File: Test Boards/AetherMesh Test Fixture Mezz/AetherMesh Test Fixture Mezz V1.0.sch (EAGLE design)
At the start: 8 parts, among them J1 POWER_JACKEJ508A, M1 AETHERMESH_MODULEMEZZ-HOLES

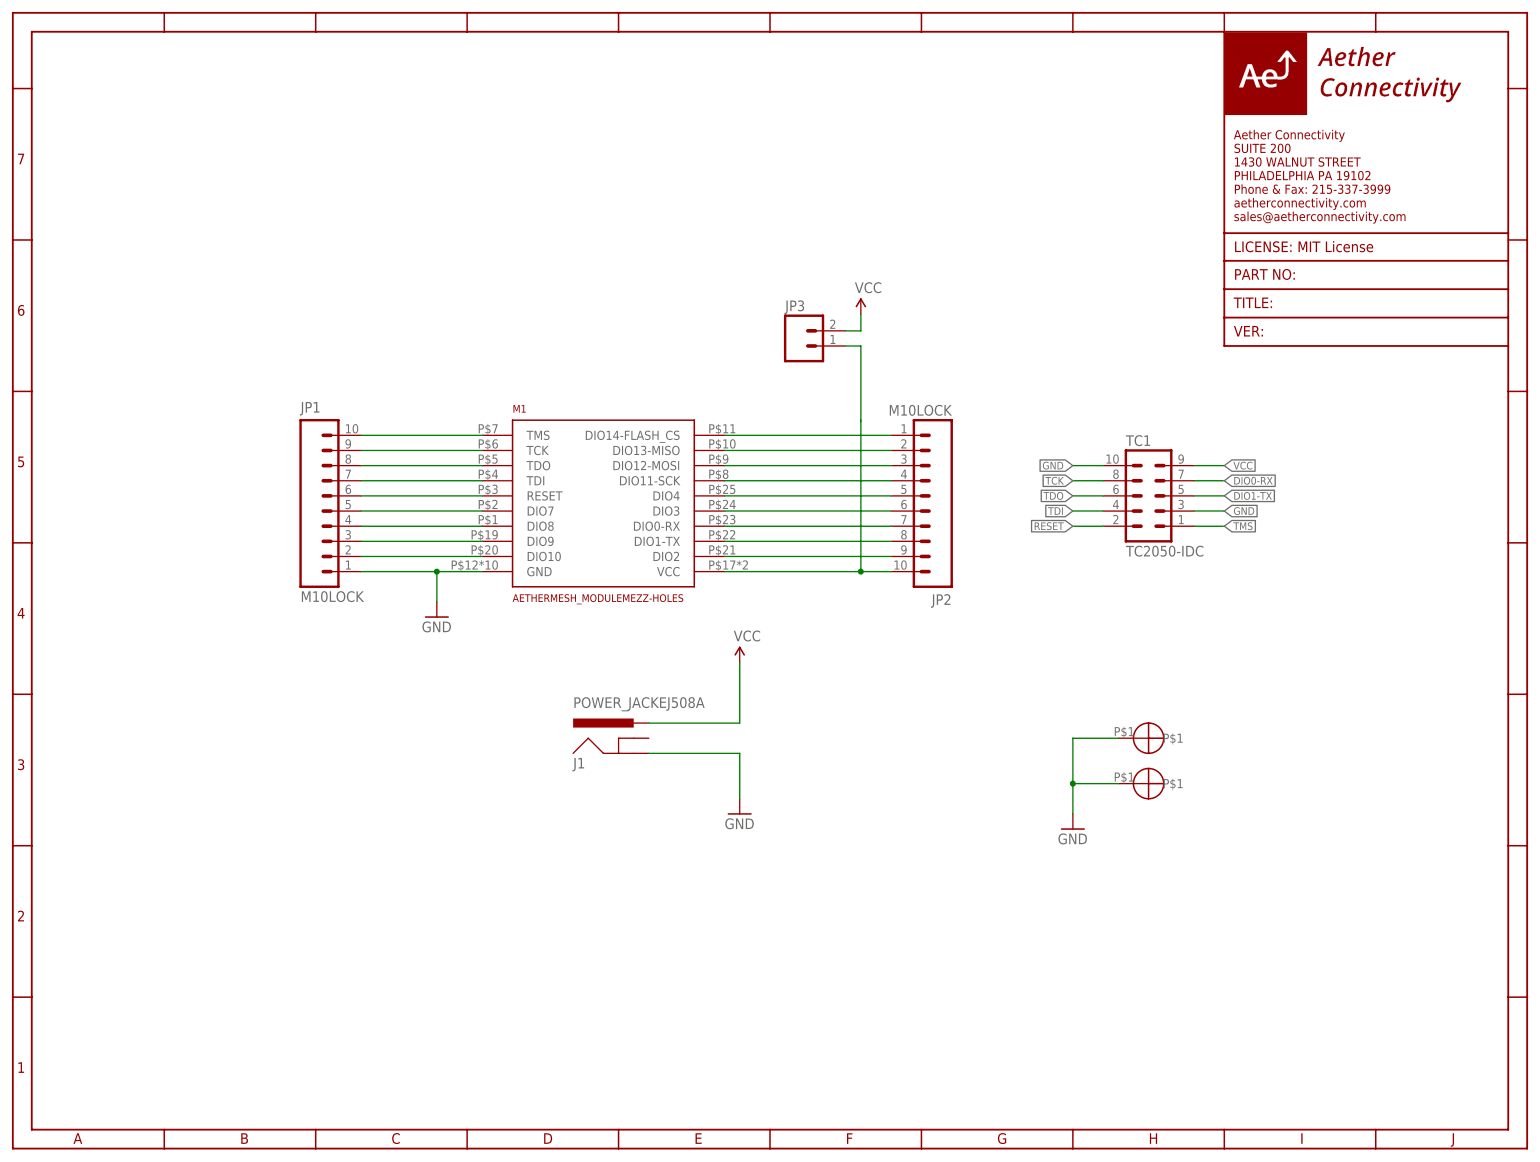
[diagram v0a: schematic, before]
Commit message: Updated reference designs and test boards with latest XDS programmer tag connect header
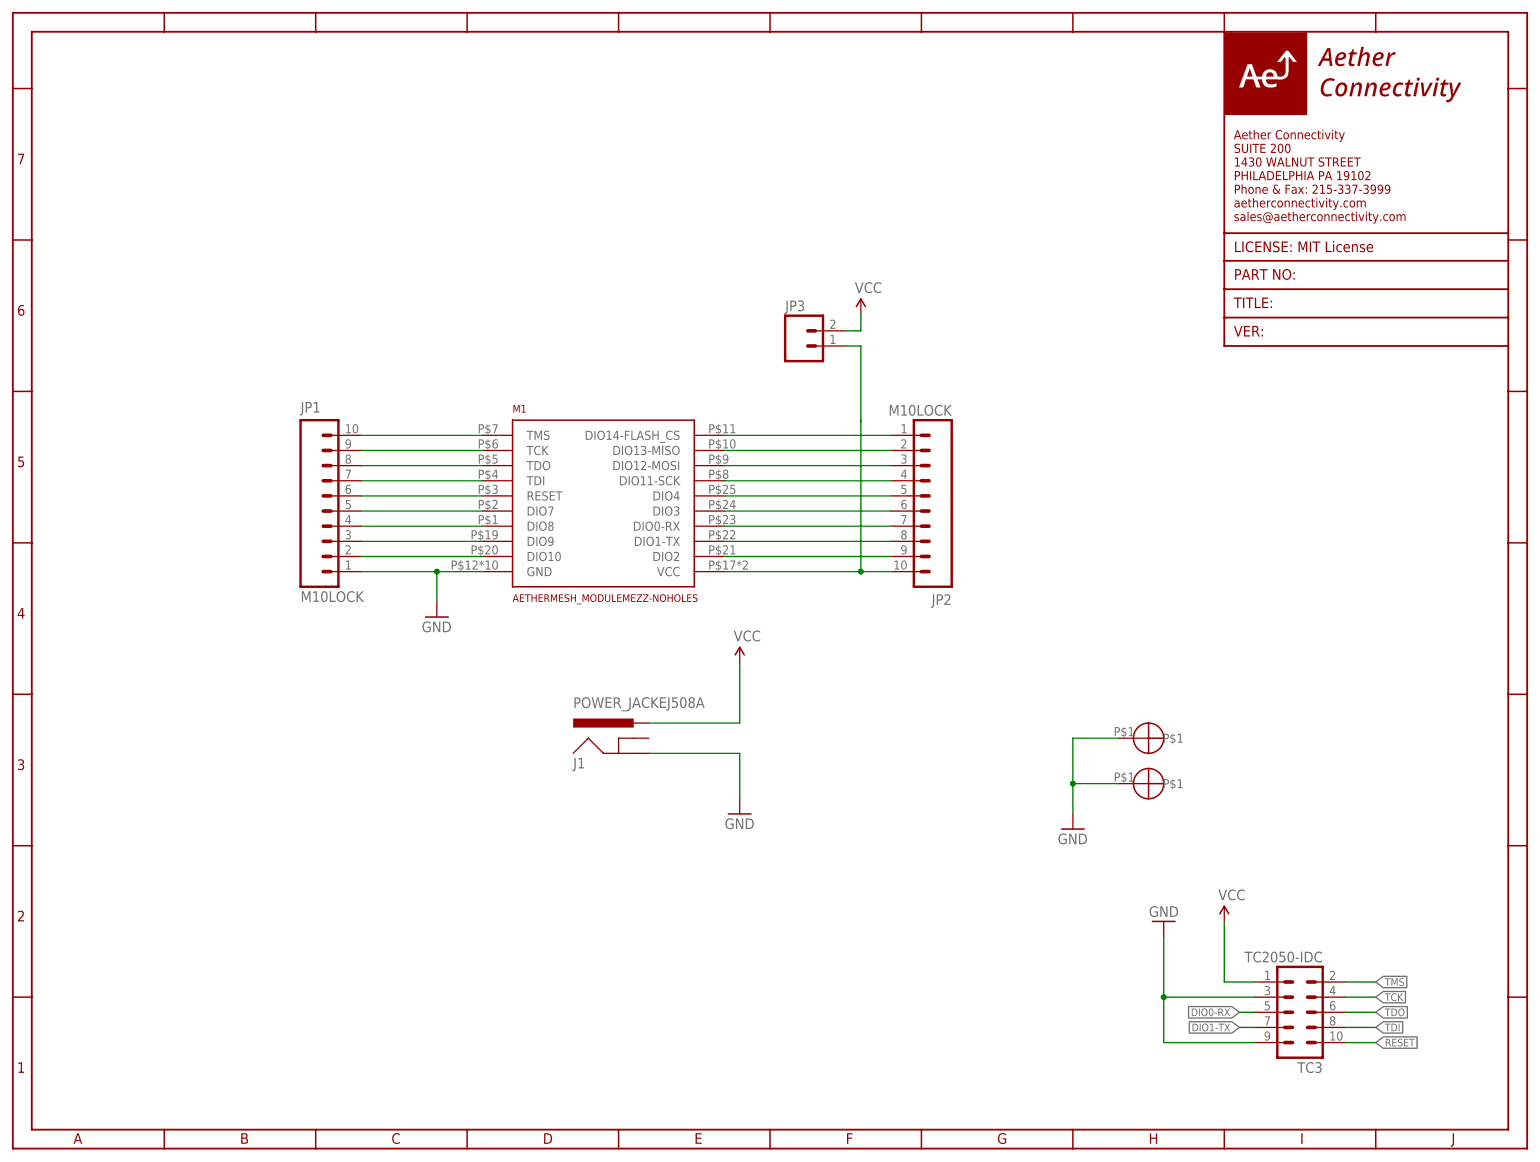
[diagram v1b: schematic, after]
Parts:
- removed TC1: TC2050-IDC, TagConnect:TC2050-IDC
- added TC3: TC2050-IDC, TagConnect:TC2050-IDC
- M1: value AETHERMESH_MODULEMEZZ-HOLES -> AETHERMESH_MODULEMEZZ-NOHOLES; device AetherConnectivity:AETHERMESH_MODULEMEZZ-HOLES -> AetherConnectivity:AETHERMESH_MODULEMEZZ-NOHOLES
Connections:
- net DIO0-RX: now also TC3.5; no longer TC1.7
- net DIO1-TX: now also TC3.7; no longer TC1.5
- net GND: now also TC3.3, TC3.9; no longer TC1.10, TC1.3
- net RESET: now also TC3.10; no longer TC1.2
- net TCK: now also TC3.4; no longer TC1.8
- net TDI: now also TC3.8; no longer TC1.4
- net TDO: now also TC3.6; no longer TC1.6
- net TMS: now also TC3.2; no longer TC1.1
- net VCC: now also TC3.1; no longer TC1.9
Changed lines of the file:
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@@
 <?xml version="1.0" encoding="utf-8"?>
 <!DOCTYPE eagle SYSTEM "eagle.dtd">
-<eagle version="8.4.1">
+<eagle version="9.0.0">
 <drawing>
 <settings>
@@
 <layer number="59" name="tCarbon" color="7" fill="1" visible="no" active="no"/>
 <layer number="60" name="bCarbon" color="7" fill="1" visible="no" active="no"/>
+<layer number="88" name="SimResults" color="9" fill="1" visible="yes" active="yes"/>
+<layer number="89" name="SimProbes" color="9" fill="1" visible="yes" active="yes"/>
 <layer number="90" name="Modules" color="5" fill="1" visible="yes" active="yes"/>
 <layer number="91" name="Nets" color="2" fill="1" visible="yes" active="yes"/>
@@
 <parts>
 <part name="GND14" library="SparkFun-Aesthetics" deviceset="GND" device=""/>
-<part name="TC1" library="TagConnect" deviceset="TC2050-IDC" device=""/>
 <part name="J1" library="3. growflux" deviceset="POWER_JACK" device="EJ508A"/>
 <part name="SUPPLY1" library="3. growflux" library_urn="urn:adsk.eagle:library:207379" deviceset="VCC" device=""/>
@@
 <part name="JP1" library="3. growflux" deviceset="M10" device="LOCK"/>
 <part name="JP2" library="3. growflux" deviceset="M10" device="LOCK"/>
-<part name="M1" library="AetherConnectivity" deviceset="AETHERMESH_MODULE" device="MEZZ-HOLES"/>
+<part name="M1" library="AetherConnectivity" deviceset="AETHERMESH_MODULE" device="MEZZ-NOHOLES" value="AETHERMESH_MODULEMEZZ-NOHOLES"/>
 <part name="S1" library="AetherConnectivity" deviceset="STANDOFF" device="WURTH">
 <attribute name="MFG#" value="9774040243R"/>
@@
 <part name="JP3" library="1. growflux" deviceset="M02" device="LOCK"/>
 <part name="SUPPLY2" library="3. growflux" library_urn="urn:adsk.eagle:library:207379" deviceset="VCC" device=""/>
+<part name="TC3" library="TagConnect" deviceset="TC2050-IDC" device=""/>
+<part name="GND3" library="SparkFun-Aesthetics" deviceset="GND" device=""/>
+<part name="SUPPLY3" library="3. growflux" library_urn="urn:adsk.eagle:library:207379" deviceset="VCC" device=""/>
 </parts>
 <sheets>
@@
 <instances>
 <instance part="GND14" gate="1" x="71.12" y="89.154"/>
-<instance part="TC1" gate="A" x="190.5" y="109.474"/>
 <instance part="J1" gate="G$1" x="104.14" y="63.754"/>
 <instance part="SUPPLY1" gate="G$1" x="121.92" y="81.534"/>
@@
 <instance part="JP3" gate="G$1" x="132.08" y="134.62"/>
 <instance part="SUPPLY2" gate="G$1" x="142.24" y="139.954"/>
+<instance part="TC3" gate="A" x="215.9" y="22.86" rot="R180"/>
+<instance part="GND3" gate="1" x="193.04" y="38.1" rot="R180"/>
+<instance part="SUPPLY3" gate="G$1" x="203.2" y="38.1"/>
 </instances>
 <busses>
@@
 <junction x="71.12" y="96.774"/>
 <pinref part="M1" gate="G$1" pin="GND"/>
-</segment>
-<segment>
-<pinref part="TC1" gate="A" pin="10"/>
-<wire x1="177.8" y1="114.554" x2="182.88" y2="114.554" width="0.1524" layer="91"/>
-<label x="177.8" y="114.554" size="1.27" layer="95" rot="R180" xref="yes"/>
-</segment>
-<segment>
-<pinref part="TC1" gate="A" pin="3"/>
-<wire x1="203.2" y1="106.934" x2="198.12" y2="106.934" width="0.1524" layer="91"/>
-<label x="203.2" y="106.934" size="1.27" layer="95" xref="yes"/>
 </segment>
 <segment>
@@
 <junction x="177.8" y="61.214"/>
 </segment>
+<segment>
+<pinref part="TC3" gate="A" pin="3"/>
+<wire x1="208.28" y1="25.4" x2="193.04" y2="25.4" width="0.1524" layer="91"/>
+<wire x1="193.04" y1="25.4" x2="193.04" y2="35.56" width="0.1524" layer="91"/>
+<pinref part="GND3" gate="1" pin="GND"/>
+<junction x="193.04" y="25.4"/>
+<pinref part="TC3" gate="A" pin="9"/>
+<wire x1="208.28" y1="17.78" x2="193.04" y2="17.78" width="0.1524" layer="91"/>
+<wire x1="193.04" y1="17.78" x2="193.04" y2="25.4" width="0.1524" layer="91"/>
+</segment>
 </net>
 <net name="VCC" class="0">
-<segment>
-<pinref part="TC1" gate="A" pin="9"/>
-<wire x1="203.2" y1="114.554" x2="198.12" y2="114.554" width="0.1524" layer="91"/>
-<label x="203.2" y="114.554" size="1.27" layer="95" xref="yes"/>
-</segment>
 <segment>
 <pinref part="J1" gate="G$1" pin="PWR"/>
@@
 <wire x1="142.24" y1="137.16" x2="142.24" y2="139.954" width="0.1524" layer="91"/>
 </segment>
+<segment>
+<pinref part="TC3" gate="A" pin="1"/>
+<wire x1="203.2" y1="27.94" x2="208.28" y2="27.94" width="0.1524" layer="91"/>
+<pinref part="SUPPLY3" gate="G$1" pin="VCC"/>
+<wire x1="203.2" y1="38.1" x2="203.2" y2="27.94" width="0.1524" layer="91"/>
+</segment>
 </net>
 <net name="ENC_RESET" class="0">
@@
 </segment>
 <segment>
-<pinref part="TC1" gate="A" pin="1"/>
-<wire x1="203.2" y1="104.394" x2="198.12" y2="104.394" width="0.1524" layer="91"/>
-<label x="203.2" y="104.394" size="1.27" layer="95" xref="yes"/>
+<pinref part="TC3" gate="A" pin="2"/>
+<wire x1="228.6" y1="27.94" x2="223.52" y2="27.94" width="0.1524" layer="91"/>
+<label x="228.6" y="27.94" size="1.27" layer="95" xref="yes"/>
 </segment>
 </net>
@@
 </segment>
 <segment>
-<pinref part="TC1" gate="A" pin="8"/>
-<wire x1="177.8" y1="112.014" x2="182.88" y2="112.014" width="0.1524" layer="91"/>
-<label x="177.8" y="112.014" size="1.27" layer="95" rot="R180" xref="yes"/>
+<pinref part="TC3" gate="A" pin="4"/>
+<wire x1="228.6" y1="25.4" x2="223.52" y2="25.4" width="0.1524" layer="91"/>
+<label x="228.6" y="25.4" size="1.27" layer="95" xref="yes"/>
 </segment>
 </net>
@@
 </segment>
 <segment>
-<pinref part="TC1" gate="A" pin="6"/>
-<wire x1="177.8" y1="109.474" x2="182.88" y2="109.474" width="0.1524" layer="91"/>
-<label x="177.8" y="109.474" size="1.27" layer="95" rot="R180" xref="yes"/>
+<pinref part="TC3" gate="A" pin="6"/>
+<wire x1="228.6" y1="22.86" x2="223.52" y2="22.86" width="0.1524" layer="91"/>
+<label x="228.6" y="22.86" size="1.27" layer="95" xref="yes"/>
 </segment>
 </net>
@@
 </segment>
 <segment>
-<pinref part="TC1" gate="A" pin="4"/>
-<wire x1="177.8" y1="106.934" x2="182.88" y2="106.934" width="0.1524" layer="91"/>
-<label x="177.8" y="106.934" size="1.27" layer="95" rot="R180" xref="yes"/>
+<pinref part="TC3" gate="A" pin="8"/>
+<wire x1="228.6" y1="20.32" x2="223.52" y2="20.32" width="0.1524" layer="91"/>
+<label x="228.6" y="20.32" size="1.27" layer="95" xref="yes"/>
 </segment>
 </net>
@@
 </segment>
 <segment>
-<pinref part="TC1" gate="A" pin="2"/>
-<wire x1="177.8" y1="104.394" x2="182.88" y2="104.394" width="0.1524" layer="91"/>
-<label x="177.8" y="104.394" size="1.27" layer="95" rot="R180" xref="yes"/>
+<pinref part="TC3" gate="A" pin="10"/>
+<wire x1="223.52" y1="17.78" x2="228.6" y2="17.78" width="0.1524" layer="91"/>
+<label x="228.6" y="17.78" size="1.27" layer="95" xref="yes"/>
 </segment>
 </net>
@@
 </segment>
 <segment>
-<pinref part="TC1" gate="A" pin="5"/>
-<wire x1="203.2" y1="109.474" x2="198.12" y2="109.474" width="0.1524" layer="91"/>
-<label x="203.2" y="109.474" size="1.27" layer="95" xref="yes"/>
+<pinref part="TC3" gate="A" pin="7"/>
+<wire x1="205.74" y1="20.32" x2="208.28" y2="20.32" width="0.1524" layer="91"/>
+<label x="205.74" y="20.32" size="1.27" layer="95" rot="R180" xref="yes"/>
 </segment>
 </net>
@@
 </segment>
 <segment>
-<pinref part="TC1" gate="A" pin="7"/>
-<wire x1="203.2" y1="112.014" x2="198.12" y2="112.014" width="0.1524" layer="91"/>
-<label x="203.2" y="112.014" size="1.27" layer="95" xref="yes"/>
-</segment>
-</net>
+<pinref part="TC3" gate="A" pin="5"/>
+<wire x1="208.28" y1="22.86" x2="205.74" y2="22.86" width="0.1524" layer="91"/>
+<label x="205.74" y="22.86" size="1.27" layer="95" rot="R180" xref="yes"/>
+</segment>
+</net>
